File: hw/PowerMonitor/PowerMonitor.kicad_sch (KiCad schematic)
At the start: 52 parts, among them J1 Conn_01x02_Socket, J2 Conn_01x02_Socket, J3 Conn_01x02_Socket, J4 Conn_01x02_Socket, J5 Conn_01x02_Socket, K1 Relay_SPST-NO, Q11 AO3400A, Q12 AO3400A, Q14 AO3400A, Q15 X0202MN, Q6 AO3400A, SW1 SW_Wuerth_450301014042, U3 LM393, U4 INA129

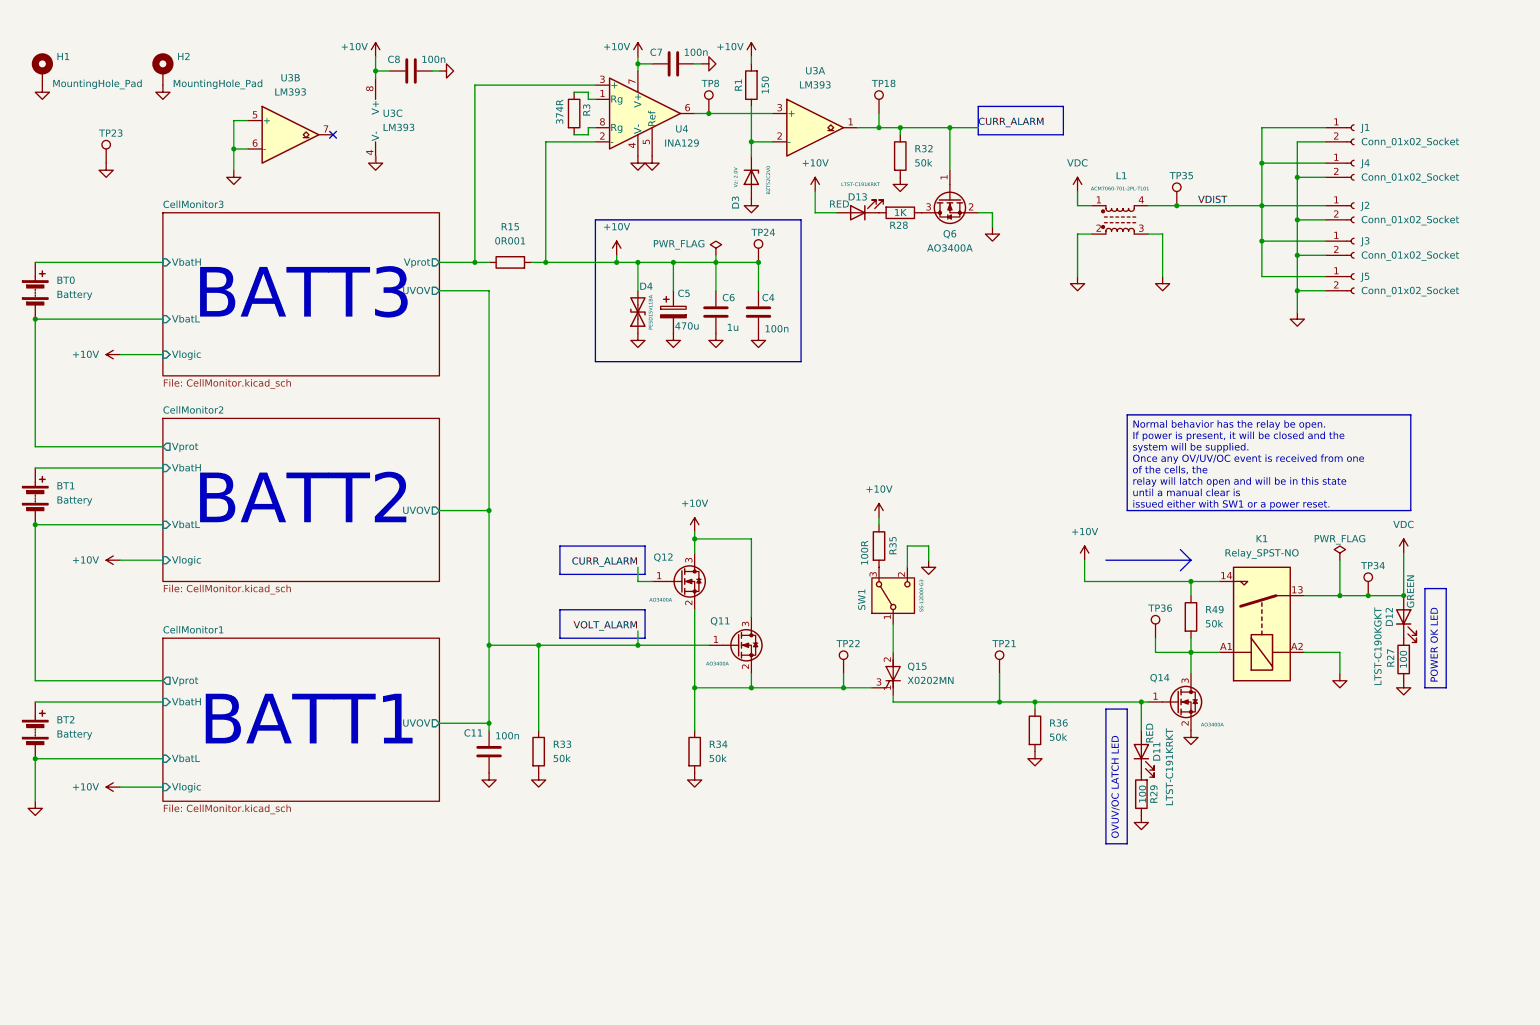
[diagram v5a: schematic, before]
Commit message: powmon: pre-fab board finishes
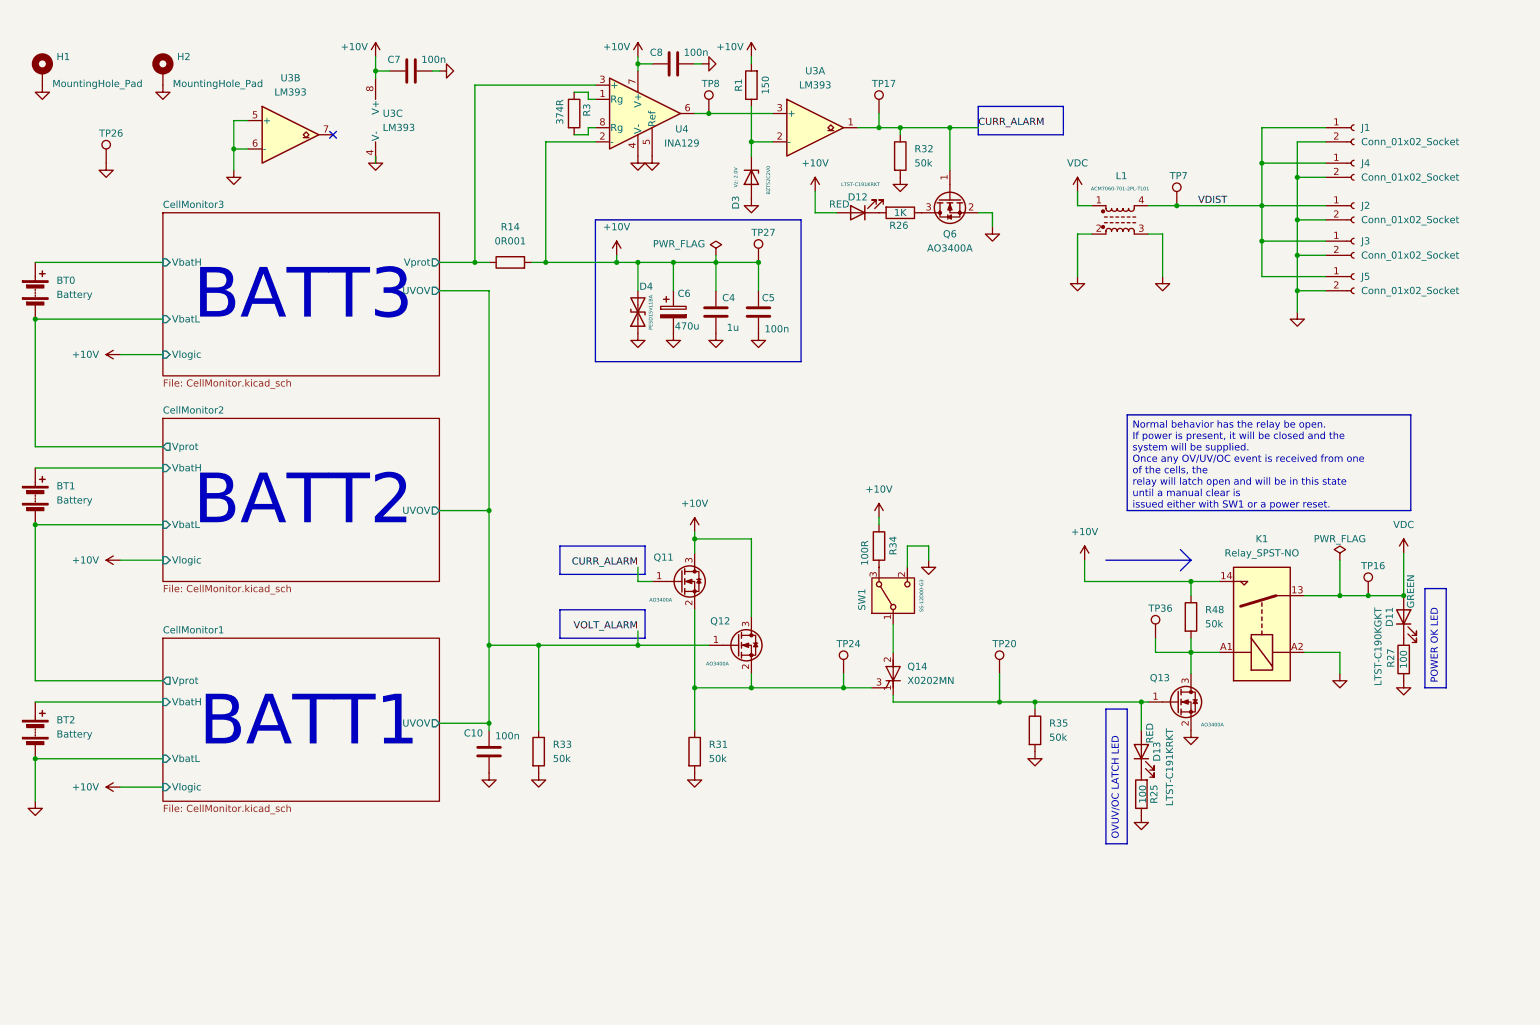
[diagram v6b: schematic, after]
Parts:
- Q14: renamed from Q15; PN (none) -> X0202MN
- renumbered C11 to C10, C6 to C4, C4 to C5, C5 to C6, C8 to C7, C7 to C8, D12 to D11, D13 to D12, D11 to D13, Q12 to Q11, Q11 to Q12, Q14 to Q13, R15 to R14, R29 to R25, R28 to R26, R34 to R31, R35 to R34, R36 to R35, R49 to R48, TP34 to TP16, TP18 to TP17, TP21 to TP20, TP22 to TP24, TP23 to TP26, TP24 to TP27, TP35 to TP7
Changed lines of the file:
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@@
 		(on_board yes)
 		(dnp no)
-		(property "Reference" "R35"
+		(property "Reference" "R34"
 			(at 171.45 107.442 90)
 			(effects
@@
 			(project "PowerMonitor"
 				(path "/7009117b-bc51-40a3-946c-93f0a2806c1b"
-					(reference "R35")
+					(reference "R34")
 					(unit 1)
 				)
@@
 		(on_board yes)
 		(dnp no)
-		(property "Reference" "C11"
+		(property "Reference" "C10"
 			(at 96.266 142.748 0)
 			(effects
@@
 			(project "PowerMonitor"
 				(path "/7009117b-bc51-40a3-946c-93f0a2806c1b"
-					(reference "C11")
+					(reference "C10")
 					(unit 1)
 				)
@@
 		(on_board yes)
 		(dnp no)
-		(property "Reference" "TP18"
+		(property "Reference" "TP17"
 			(at 167.64 26.416 0)
 			(effects
@@
 			(project "PowerMonitor"
 				(path "/7009117b-bc51-40a3-946c-93f0a2806c1b"
-					(reference "TP18")
+					(reference "TP17")
 					(unit 1)
 				)
@@
 		(on_board yes)
 		(dnp no)
-		(property "Reference" "C8"
+		(property "Reference" "C7"
 			(at 82.042 22.098 90)
 			(effects
@@
 			(project "PowerMonitor"
 				(path "/7009117b-bc51-40a3-946c-93f0a2806c1b"
-					(reference "C8")
+					(reference "C7")
 					(unit 1)
 				)
@@
 		(dnp no)
 		(fields_autoplaced yes)
-		(property "Reference" "R49"
+		(property "Reference" "R48"
 			(at 227.33 120.6499 0)
 			(effects
@@
 			(project "PowerMonitor"
 				(path "/7009117b-bc51-40a3-946c-93f0a2806c1b"
-					(reference "R49")
+					(reference "R48")
 					(unit 1)
 				)
@@
 		(dnp no)
 		(fields_autoplaced yes)
-		(property "Reference" "R15"
+		(property "Reference" "R14"
 			(at 102.87 52.07 90)
 			(effects
@@
 			(project ""
 				(path "/7009117b-bc51-40a3-946c-93f0a2806c1b"
-					(reference "R15")
+					(reference "R14")
 					(unit 1)
 				)
@@
 		(on_board yes)
 		(dnp no)
-		(property "Reference" "D11"
+		(property "Reference" "D13"
 			(at 218.694 146.05 0)
 			(effects
@@
 			(project "PowerMonitor"
 				(path "/7009117b-bc51-40a3-946c-93f0a2806c1b"
-					(reference "D11")
+					(reference "D13")
 					(unit 1)
 				)
@@
 		(on_board yes)
 		(dnp no)
-		(property "Reference" "Q12"
+		(property "Reference" "Q11"
 			(at 128.524 111.252 0)
 			(effects
@@
 			(project "PowerMonitor"
 				(path "/7009117b-bc51-40a3-946c-93f0a2806c1b"
-					(reference "Q12")
+					(reference "Q11")
 					(unit 1)
 				)
@@
 		(on_board yes)
 		(dnp no)
-		(property "Reference" "TP22"
+		(property "Reference" "TP24"
 			(at 161.29 126.746 0)
 			(effects
@@
 			(project "PowerMonitor"
 				(path "/7009117b-bc51-40a3-946c-93f0a2806c1b"
-					(reference "TP22")
+					(reference "TP24")
 					(unit 1)
 				)
@@
 		(on_board yes)
 		(dnp no)
-		(property "Reference" "C5"
+		(property "Reference" "C6"
 			(at 132.842 64.008 0)
 			(effects
@@
 			(project ""
 				(path "/7009117b-bc51-40a3-946c-93f0a2806c1b"
-					(reference "C5")
+					(reference "C6")
 					(unit 1)
 				)
@@
 		(on_board yes)
 		(dnp no)
-		(property "Reference" "Q14"
+		(property "Reference" "Q13"
 			(at 217.424 132.842 0)
 			(effects
@@
 			(project "PowerMonitor"
 				(path "/7009117b-bc51-40a3-946c-93f0a2806c1b"
-					(reference "Q14")
+					(reference "Q13")
 					(unit 1)
 				)
@@
 		(on_board yes)
 		(dnp no)
-		(property "Reference" "R29"
+		(property "Reference" "R25"
 			(at 218.186 153.67 90)
 			(effects
@@
 			(project "PowerMonitor"
 				(path "/7009117b-bc51-40a3-946c-93f0a2806c1b"
-					(reference "R29")
+					(reference "R25")
 					(unit 1)
 				)
@@
 		(on_board yes)
 		(dnp no)
-		(property "Reference" "Q11"
+		(property "Reference" "Q12"
 			(at 138.684 122.682 0)
 			(effects
@@
 			(project "PowerMonitor"
 				(path "/7009117b-bc51-40a3-946c-93f0a2806c1b"
-					(reference "Q11")
+					(reference "Q12")
 					(unit 1)
 				)
@@
 		(on_board yes)
 		(dnp no)
-		(property "Reference" "TP35"
+		(property "Reference" "TP7"
 			(at 220.98 42.926 0)
 			(effects
@@
 			(project "PowerMonitor"
 				(path "/7009117b-bc51-40a3-946c-93f0a2806c1b"
-					(reference "TP35")
+					(reference "TP7")
 					(unit 1)
 				)
@@
 		(on_board yes)
 		(dnp no)
-		(property "Reference" "C7"
+		(property "Reference" "C8"
 			(at 129.032 20.828 90)
 			(effects
@@
 			(project "PowerMonitor"
 				(path "/7009117b-bc51-40a3-946c-93f0a2806c1b"
-					(reference "C7")
+					(reference "C8")
 					(unit 1)
 				)
@@
 		(dnp no)
 		(fields_autoplaced yes)
-		(property "Reference" "Q15"
+		(property "Reference" "Q14"
 			(at 173.99 130.8099 0)
 			(effects
@@
 			)
 		)
+		(property "PN" "X0202MN"
+			(at 171.45 132.08 0)
+			(effects
+				(font
+					(size 1.27 1.27)
+				)
+				(hide yes)
+			)
+		)
 		(pin "3"
 		)
@@
 			(project ""
 				(path "/7009117b-bc51-40a3-946c-93f0a2806c1b"
-					(reference "Q15")
+					(reference "Q14")
 					(unit 1)
 				)
@@
 		(on_board yes)
 		(dnp no)
-		(property "Reference" "TP21"
+		(property "Reference" "TP20"
 			(at 189.23 126.746 0)
 			(effects
@@
 			(project "PowerMonitor"
 				(path "/7009117b-bc51-40a3-946c-93f0a2806c1b"
-					(reference "TP21")
+					(reference "TP20")
 					(unit 1)
 				)
@@
 		(on_board yes)
 		(dnp no)
-		(property "Reference" "TP23"
+		(property "Reference" "TP26"
 			(at 29.21 35.306 0)
 			(effects
@@
 			(project "PowerMonitor"
 				(path "/7009117b-bc51-40a3-946c-93f0a2806c1b"
-					(reference "TP23")
+					(reference "TP26")
 					(unit 1)
 				)
@@
 		(on_board yes)
 		(dnp no)
-		(property "Reference" "D13"
+		(property "Reference" "D12"
 			(at 165.1 46.736 0)
 			(effects
@@
 			(project "PowerMonitor"
 				(path "/7009117b-bc51-40a3-946c-93f0a2806c1b"
-					(reference "D13")
+					(reference "D12")
 					(unit 1)
 				)
@@
 		(on_board yes)
 		(dnp no)
-		(property "Reference" "C6"
+		(property "Reference" "C4"
 			(at 141.986 64.77 0)
 			(effects
@@
 			(project "PowerMonitor"
 				(path "/7009117b-bc51-40a3-946c-93f0a2806c1b"
-					(reference "C6")
+					(reference "C4")
 					(unit 1)
 				)
@@
 		(on_board yes)
 		(dnp no)
-		(property "Reference" "C4"
+		(property "Reference" "C5"
 			(at 149.098 64.77 0)
 			(effects
@@
 			(project "PowerMonitor"
 				(path "/7009117b-bc51-40a3-946c-93f0a2806c1b"
-					(reference "C4")
+					(reference "C5")
 					(unit 1)
 				)
@@
 		(on_board yes)
 		(dnp no)
-		(property "Reference" "R28"
+		(property "Reference" "R26"
 			(at 172.466 51.816 90)
 			(effects
@@
 			(project "PowerMonitor"
 				(path "/7009117b-bc51-40a3-946c-93f0a2806c1b"
-					(reference "R28")
+					(reference "R26")
 					(unit 1)
 				)
@@
 		(on_board yes)
 		(dnp no)
-		(property "Reference" "D12"
+		(property "Reference" "D11"
 			(at 260.35 121.92 0)
 			(effects
@@
 			(project "PowerMonitor"
 				(path "/7009117b-bc51-40a3-946c-93f0a2806c1b"
-					(reference "D12")
+					(reference "D11")
 					(unit 1)
 				)
@@
 		(dnp no)
 		(fields_autoplaced yes)
-		(property "Reference" "R36"
+		(property "Reference" "R35"
 			(at 199.39 140.9699 0)
 			(effects
@@
 			(project "PowerMonitor"
 				(path "/7009117b-bc51-40a3-946c-93f0a2806c1b"
-					(reference "R36")
+					(reference "R35")
 					(unit 1)
 				)
@@
 		(dnp no)
 		(fields_autoplaced yes)
-		(property "Reference" "R34"
+		(property "Reference" "R31"
 			(at 138.43 144.7799 0)
 			(effects
@@
 			(project "PowerMonitor"
 				(path "/7009117b-bc51-40a3-946c-93f0a2806c1b"
-					(reference "R34")
+					(reference "R31")
 					(unit 1)
 				)
@@
 		(on_board yes)
 		(dnp no)
-		(property "Reference" "TP24"
+		(property "Reference" "TP27"
 			(at 146.05 53.086 0)
 			(effects
@@
 			(project "PowerMonitor"
 				(path "/7009117b-bc51-40a3-946c-93f0a2806c1b"
-					(reference "TP24")
+					(reference "TP27")
 					(unit 1)
 				)
@@
 		(on_board yes)
 		(dnp no)
-		(property "Reference" "TP34"
+		(property "Reference" "TP16"
 			(at 255.27 112.776 0)
 			(effects
@@
 			(project "PowerMonitor"
 				(path "/7009117b-bc51-40a3-946c-93f0a2806c1b"
-					(reference "TP34")
+					(reference "TP16")
 					(unit 1)
 				)

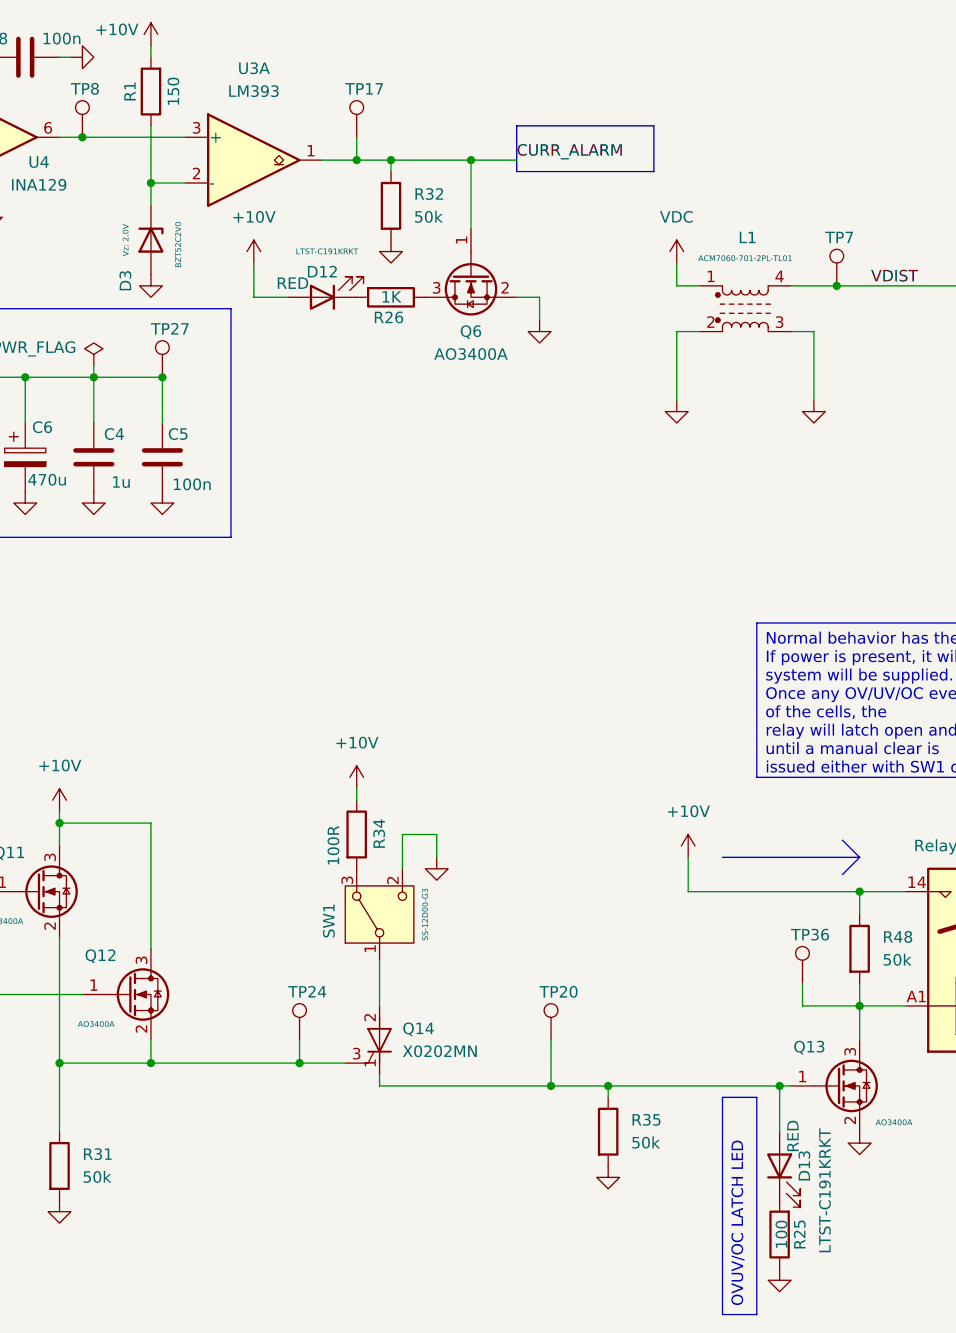
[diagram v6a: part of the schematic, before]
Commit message: powmon: change plane connections to solid and add vias
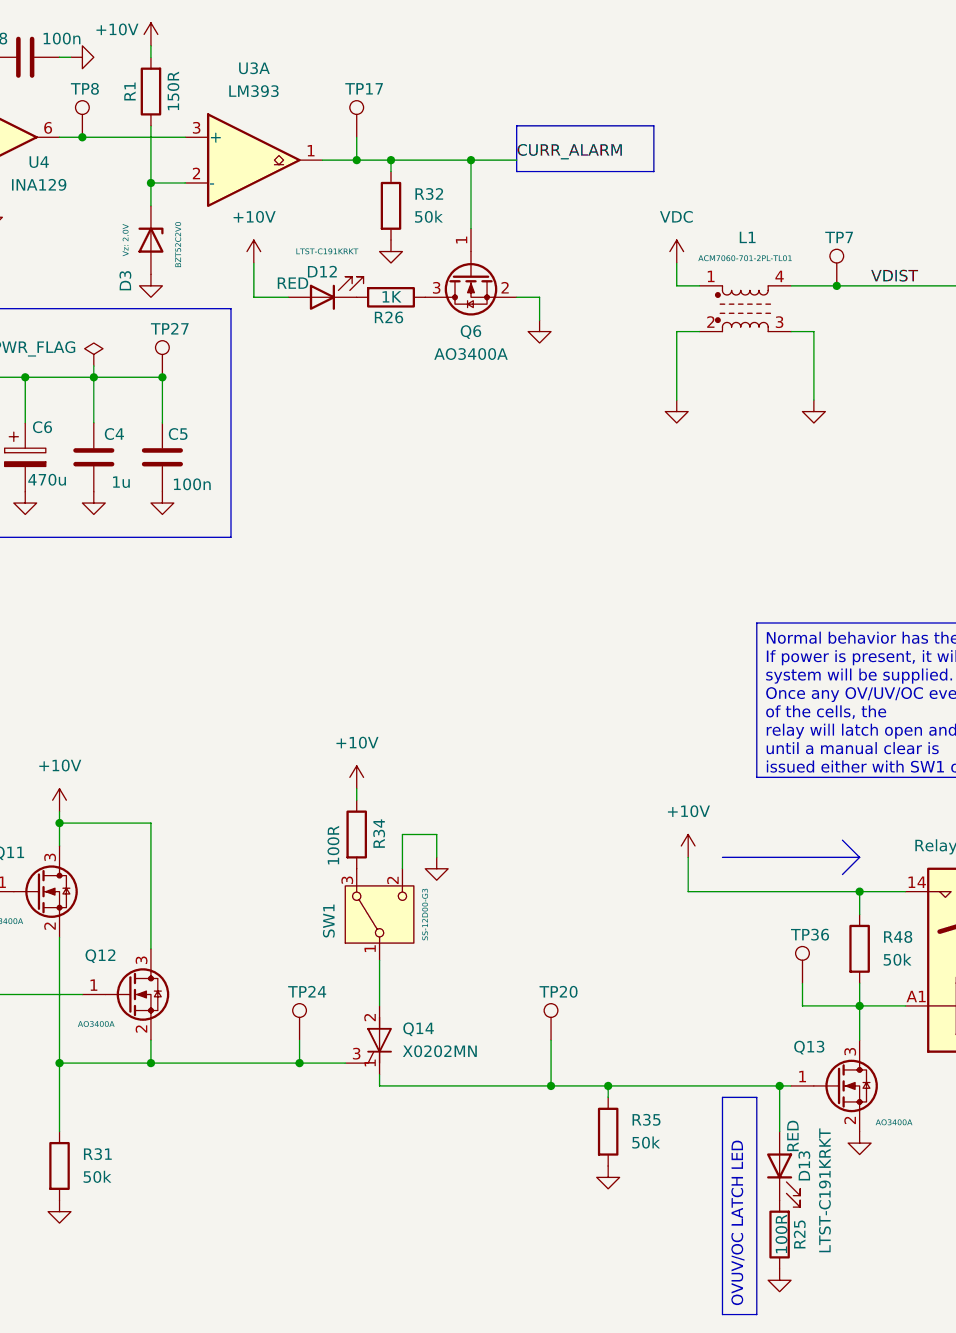
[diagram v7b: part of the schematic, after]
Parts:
- C6: footprint Capacitor_THT:CP_Radial_D4.0mm_P1.50mm -> Capacitor_THT:CP_Radial_D8.0mm_P5.00mm; PN (none) -> 470UF25VG130GF
- R1: value 150 -> 150R
- R25: value 100 -> 100R
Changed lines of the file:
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@@
 			)
 		)
-		(property "Footprint" "Capacitor_THT:CP_Radial_D4.0mm_P1.50mm"
+		(property "Footprint" "Capacitor_THT:CP_Radial_D8.0mm_P5.00mm"
 			(at 133.0452 71.12 0)
 			(effects
@@
 		)
 		(property "Description" "Polarized capacitor"
+			(at 132.08 67.31 0)
+			(effects
+				(font
+					(size 1.27 1.27)
+				)
+				(hide yes)
+			)
+		)
+		(property "PN" "470UF25VG130GF"
 			(at 132.08 67.31 0)
 			(effects
@@
 			)
 		)
-		(property "Value" "100"
+		(property "Value" "100R"
 			(at 216.154 153.67 90)
 			(effects
@@
 			)
 		)
-		(property "Value" "150"
+		(property "Value" "150R"
 			(at 148.59 26.67 90)
 			(effects
